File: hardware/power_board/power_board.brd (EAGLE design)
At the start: 53 x 70 mm, 36 parts, among them J5 20021311-00010T4LF, J6 20021311-00010T4LF, J7 20021311-00010T4LF, Q1 600mA/40V, Q3 600mA/40V, Q4 NTMD4184PFR2G, U11 INA219AIDCNR, U5 POLOLU_STEPUP_U1V11X

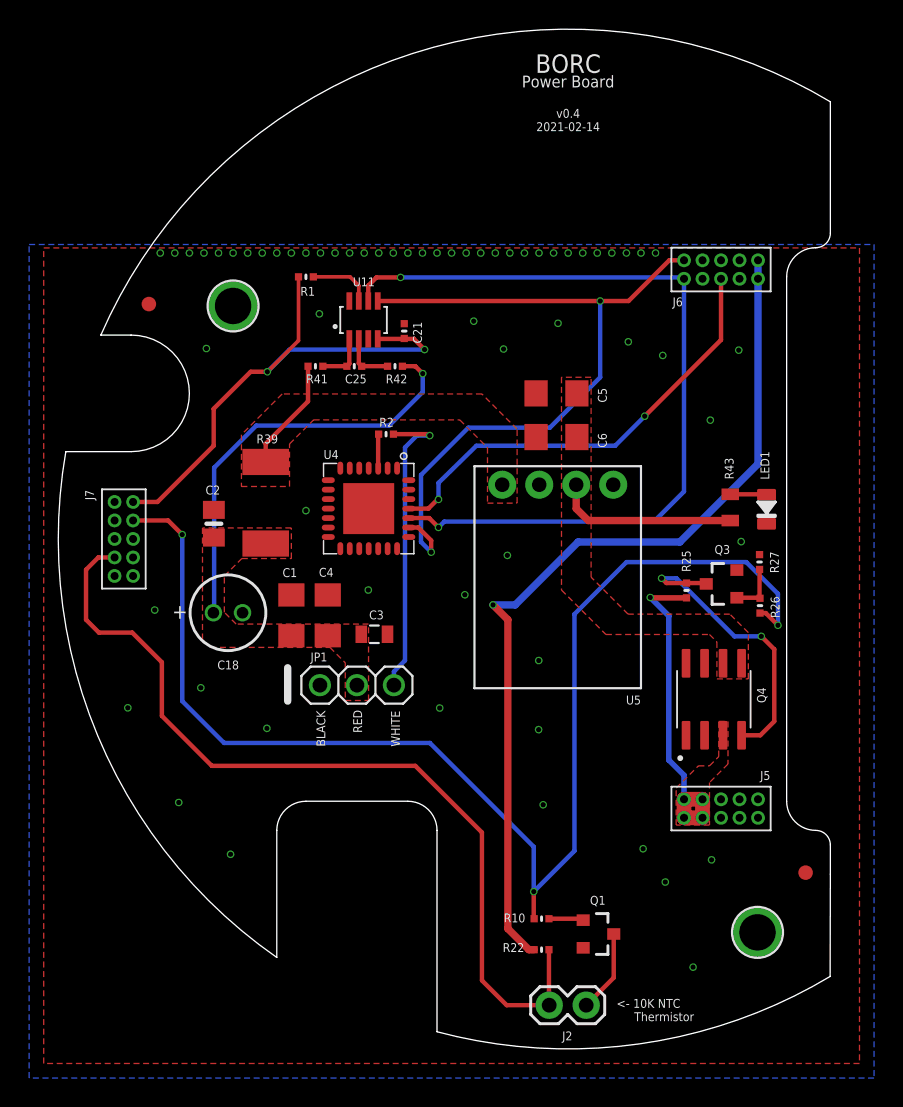
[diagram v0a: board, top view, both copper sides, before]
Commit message: power board upgraded to v0.5
- added footprint for Pololu U3V40F5
- thickened several power traces even more
- added flyback diode to 5V line
- rearranged some traces to accommodate mods
- updated schematic, gerbers, render, dimensions
- ERC/DRC
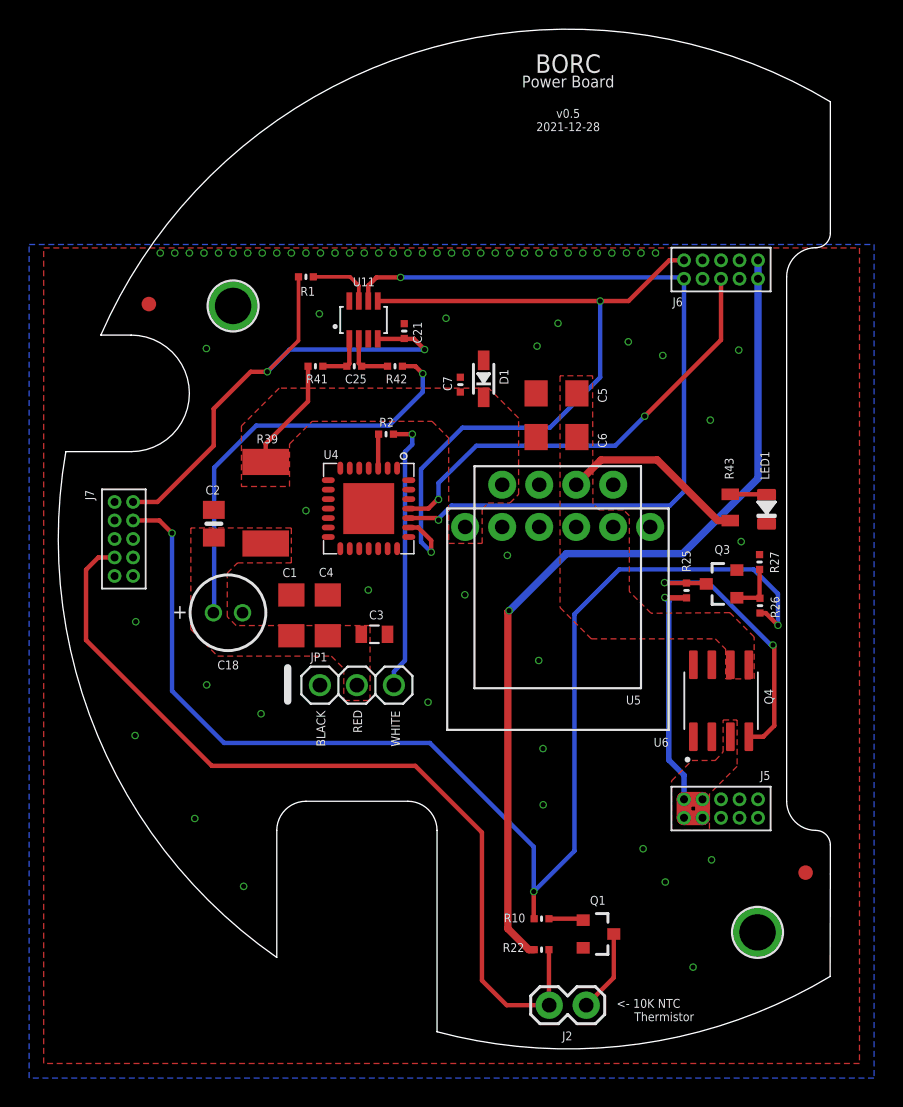
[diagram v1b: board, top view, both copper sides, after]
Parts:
- added C7: 0.1uF, Adafruit Feather 32u4 Bluefruit LE:MICROBUILDER__0402MP
- added D1: 1N4148, microbuilder:SOD-323
- added U6: POLOLU_STEPUP_U3V40X, Pololu Step Up Vregs:POLOLU_STEPUP_U3V40X
- moved Q4 0.51 mm to (45.5, 23.9)
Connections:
- net 5V: now also C7.1, D1.C, U6.VOUT
- net GND: now also C7.2, D1.A, U6.GND@1, U6.GND@2
- net VBAT_ON: now also U6.VIN@1, U6.VIN@2
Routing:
- net CH0: track 21.2 -> 19.0 mm
- net VBAT: track 22.4 -> 21.0 mm
- net TEMP: track 60.4 -> 59.1 mm
- net VCC: track 61.2 -> 60.1 mm
- net N$32: track 20.6 -> 19.7 mm
- net MOTOR_CONTROL: track 88.7 -> 88.0 mm
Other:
- board text added: "v0.5 2021-12-28"
- board text removed: "v0.4 2021-02-14"
